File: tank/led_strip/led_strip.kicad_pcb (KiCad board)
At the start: 2 copper layers, 50.5 x 10.8 mm, 9 parts, among them J1 Conn_01x04_Male

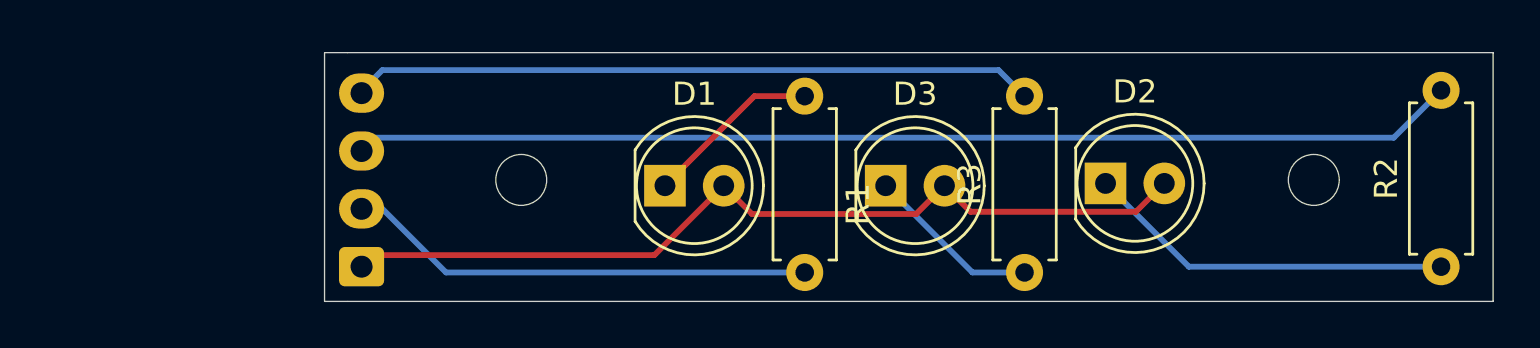
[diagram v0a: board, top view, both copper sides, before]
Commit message: LED Strip v0.5 - Change LED strip from 3 LEDs to 4
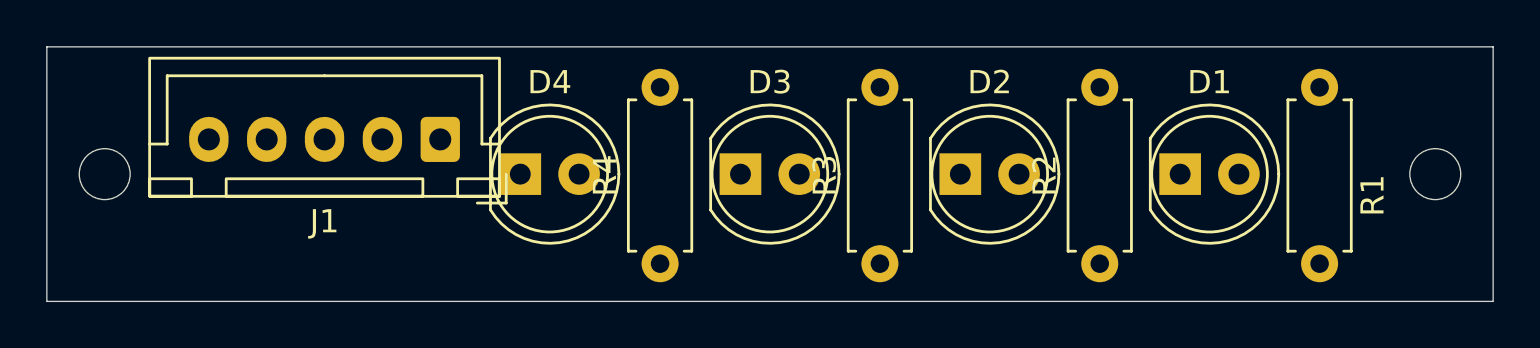
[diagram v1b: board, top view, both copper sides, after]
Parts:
- removed REF** (x2): MountingHole_2.2mm_M2, MountingHole:MountingHole_2.2mm_M2
- added D4: LED, custom:LED_D5.0mm, F.Cu at (101.5, 97.5)
- added H1: MountingHole, MountingHole:MountingHole_2.2mm_M2, F.Cu at (83.5, 97.5)
- added H2: MountingHole, MountingHole:MountingHole_2.2mm_M2, F.Cu at (141.0, 97.5)
- added R4: R, custom:R_Axial_DIN0207_L6.3mm_D2.5mm_P7.62mm_Horizontal, F.Cu at (107.5, 101.4)
- J1: value Conn_01x04_Male -> Conn_01x05_Pin; footprint custom:JST_EH_B4B-EH-A_1x04_P2.50mm_Vertical -> Connector_JST:JST_XH_B5B-XH-A_1x05_P2.50mm_Vertical; moved to F.Cu
- moved D1 22.3 mm to (130.0, 97.5)
- moved R1 22.3 mm to (136.0, 93.8)
- moved R2 14.8 mm to (126.5, 101.4)
- moved J1 6.47 mm to (98.0, 96.0), turned to 180 degrees
- moved D3 6.29 mm to (111.0, 97.5)
- moved D2 6.29 mm to (120.5, 97.5)
- moved R3 6.26 mm to (117.0, 101.4)
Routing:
- net Net-(J1-Pin_3): track 47.1 -> 0.00 mm
- net Net-(D1-A): track 37.5 -> 0.00 mm
- net Net-(J1-Pin_4): track 28.9 -> 0.00 mm
- net Net-(J1-Pin_2): track 20.1 -> 0.00 mm
- net Net-(D2-K): track 16.0 -> 0.00 mm
- net Net-(D1-K): track 7.64 -> 0.00 mm
- net Net-(D3-K): track 7.55 -> 0.00 mm
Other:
- board size 50.5 x 10.8 mm -> 62.5 x 11 mm
- net class Default removed
- board text added: "LED Strip Version 0.5"
- board text removed: "LED Strip Version 0.4"

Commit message: whoops!
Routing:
- net Net-(J1-Pin_2): track 0.00 -> 42.7 mm
- net Net-(D1-A): track 0.00 -> 41.5 mm
- net Net-(J1-Pin_3): track 0.00 -> 35.4 mm
- net Net-(J1-Pin_4): track 0.00 -> 27.6 mm
- net Net-(J1-Pin_5): track 0.00 -> 20.4 mm
- net Net-(D4-K): track 0.00 -> 7.64 mm
- net Net-(D3-K): track 0.00 -> 7.63 mm
- net Net-(D2-K): track 0.00 -> 7.63 mm
- net Net-(D1-K): track 0.00 -> 7.58 mm
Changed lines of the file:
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@@
 		)
+	)
+	(segment
+		(start 104 97.5)
+		(end 102.5 96)
+		(width 0.25)
+		(layer "F.Cu")
+		(net 1)
+	)
+	(segment
+		(start 113.515 97.5)
+		(end 112.015 96)
+		(width 0.25)
+		(layer "F.Cu")
+		(net 1)
+	)
+	(segment
+		(start 112.015 96)
+		(end 121.515 96)
+		(width 0.25)
+		(layer "F.Cu")
+		(net 1)
+	)
+	(segment
+		(start 121.515 96)
+		(end 123.015 97.5)
+		(width 0.25)
+		(layer "F.Cu")
+		(net 1)
+	)
+	(segment
+		(start 112.015 96)
+		(end 102.5 96)
+		(width 0.25)
+		(layer "F.Cu")
+		(net 1)
+	)
+	(segment
+		(start 102.5 96)
+		(end 98 96)
+		(width 0.25)
+		(layer "F.Cu")
+		(net 1)
+	)
+	(segment
+		(start 131.015 96)
+		(end 132.515 97.5)
+		(width 0.25)
+		(layer "F.Cu")
+		(net 1)
+	)
+	(segment
+		(start 121.515 96)
+		(end 131.015 96)
+		(width 0.25)
+		(layer "F.Cu")
+		(net 1)
+	)
+	(segment
+		(start 133.725 93.75)
+		(end 136 93.75)
+		(width 0.25)
+		(layer "B.Cu")
+		(net 2)
+	)
+	(segment
+		(start 129.975 97.5)
+		(end 133.725 93.75)
+		(width 0.25)
+		(layer "B.Cu")
+		(net 2)
+	)
+	(segment
+		(start 124.345 101.37)
+		(end 126.5 101.37)
+		(width 0.25)
+		(layer "F.Cu")
+		(net 3)
+	)
+	(segment
+		(start 120.475 97.5)
+		(end 124.345 101.37)
+		(width 0.25)
+		(layer "F.Cu")
+		(net 3)
+	)
+	(segment
+		(start 110.975 97.5)
+		(end 114.845 101.37)
+		(width 0.25)
+		(layer "F.Cu")
+		(net 4)
+	)
+	(segment
+		(start 114.845 101.37)
+		(end 117 101.37)
+		(width 0.25)
+		(layer "F.Cu")
+		(net 4)
+	)
+	(segment
+		(start 105.33 101.37)
+		(end 107.5 101.37)
+		(width 0.25)
+		(layer "F.Cu")
+		(net 5)
+	)
+	(segment
+		(start 101.46 97.5)
+		(end 105.33 101.37)
+		(width 0.25)
+		(layer "F.Cu")
+		(net 5)
+	)
+	(segment
+		(start 99.744 100.244)
+		(end 95.5 96)
+		(width 0.25)
+		(layer "B.Cu")
+		(net 6)
+	)
+	(segment
+		(start 136 101.37)
+		(end 134.874 100.244)
+		(width 0.25)
+		(layer "B.Cu")
+		(net 6)
+	)
+	(segment
+		(start 134.874 100.244)
+		(end 99.744 100.244)
+		(width 0.25)
+		(layer "B.Cu")
+		(net 6)
+	)
+	(segment
+		(start 93 96)
+		(end 96.376 92.624)
+		(width 0.25)
+		(layer "B.Cu")
+		(net 7)
+	)
+	(segment
+		(start 96.376 92.624)
+		(end 125.374 92.624)
+		(width 0.25)
+		(layer "B.Cu")
+		(net 7)
+	)
+	(segment
+		(start 125.374 92.624)
+		(end 126.5 93.75)
+		(width 0.25)
+		(layer "B.Cu")
+		(net 7)
+	)
+	(segment
+		(start 91.801 94.699)
+		(end 106.856595 94.699)
+		(width 0.25)
+		(layer "F.Cu")
+		(net 8)
+	)
+	(segment
+		(start 107.033595 94.876)
+		(end 115.874 94.876)
+		(width 0.25)
+		(layer "F.Cu")
+		(net 8)
+	)
+	(segment
+		(start 115.874 94.876)
+		(end 117 93.75)
+		(width 0.25)
+		(layer "F.Cu")
+		(net 8)
+	)
+	(segment
+		(start 106.856595 94.699)
+		(end 107.033595 94.876)
+		(width 0.25)
+		(layer "F.Cu")
+		(net 8)
+	)
+	(segment
+		(start 90.5 96)
+		(end 91.801 94.699)
+		(width 0.25)
+		(layer "F.Cu")
+		(net 8)
+	)
+	(segment
+		(start 88 96)
+		(end 90.25 93.75)
+		(width 0.25)
+		(layer "F.Cu")
+		(net 9)
+	)
+	(segment
+		(start 90.25 93.75)
+		(end 107.5 93.75)
+		(width 0.25)
+		(layer "F.Cu")
+		(net 9)
 	)
 	(embedded_fonts no)

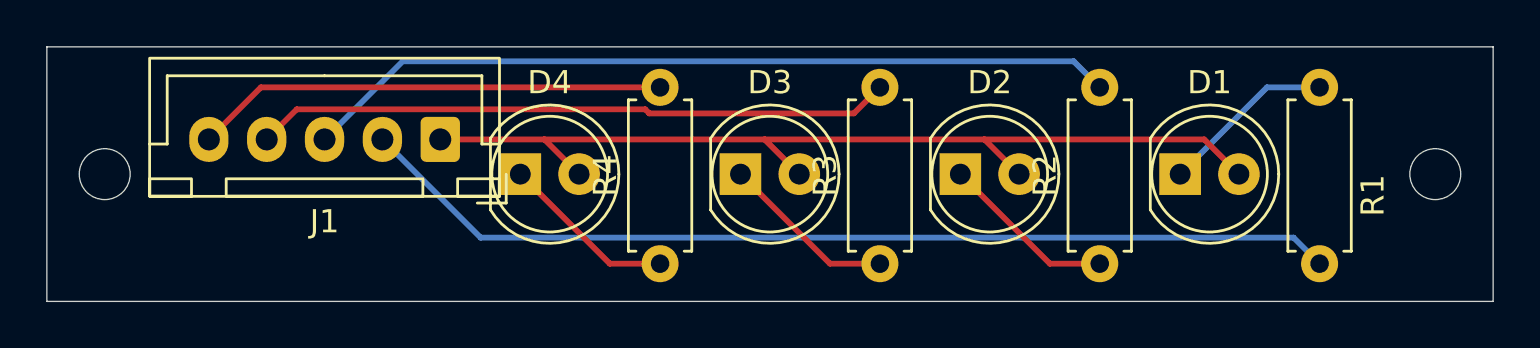
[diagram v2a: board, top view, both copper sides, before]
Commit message: LED Strip v0.6
Different spacing for LEDs
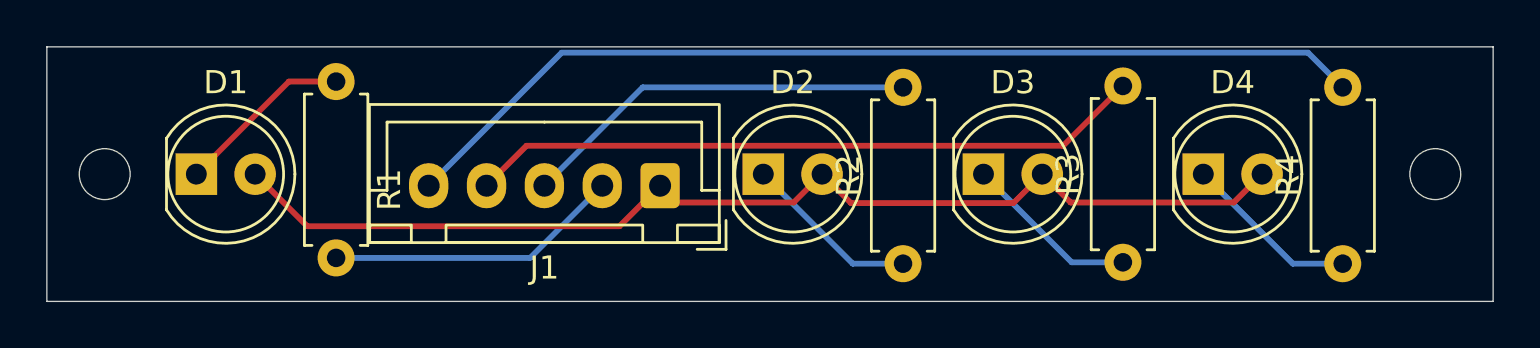
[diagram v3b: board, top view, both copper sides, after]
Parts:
- moved D1 42.5 mm to (87.5, 97.5)
- moved R1 42.5 mm to (93.5, 93.5)
- moved D4 29.5 mm to (131.0, 97.5)
- moved R4 29.5 mm to (137.0, 101.4)
- moved R3 10.5 mm to (127.5, 101.3)
- moved D3 10.5 mm to (121.5, 97.5)
- moved J1 9.71 mm to (107.5, 98.0)
- moved D2 8.52 mm to (112.0, 97.5)
- moved R2 8.50 mm to (118.0, 101.4)
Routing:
- net Net-(J1-Pin_2): track 42.7 -> 12.8 mm
- net Net-(J1-Pin_5): track 20.4 -> 42.5 mm
- net Net-(J1-Pin_3): track 35.4 -> 17.3 mm
- net Net-(D1-A): track 41.5 -> 48.0 mm
- net Net-(J1-Pin_4): track 27.6 -> 29.3 mm
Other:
- board text added: "LED Strip Version 0.6"
- board text removed: "LED Strip Version 0.5"
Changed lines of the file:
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@@
 	(footprint "custom:LED_D5.0mm"
 		(layer "F.Cu")
-		(at 129.975 97.5)
+		(at 87.46 97.5)
 		(descr "LED, diameter 5.0mm, 2 pins, http://cdn-reichelt.de/documents/datenblatt/A500/LL-504BC2E-009.pdf")
 		(tags "LED diameter 5.0mm 2 pins")
@@
 	(footprint "custom:LED_D5.0mm"
 		(layer "F.Cu")
-		(at 120.475 97.5)
+		(at 111.96 97.5)
 		(descr "LED, diameter 5.0mm, 2 pins, http://cdn-reichelt.de/documents/datenblatt/A500/LL-504BC2E-009.pdf")
 		(tags "LED diameter 5.0mm 2 pins")
@@
 	(footprint "custom:LED_D5.0mm"
 		(layer "F.Cu")
-		(at 110.975 97.5)
+		(at 121.475 97.5)
 		(descr "LED, diameter 5.0mm, 2 pins, http://cdn-reichelt.de/documents/datenblatt/A500/LL-504BC2E-009.pdf")
 		(tags "LED diameter 5.0mm 2 pins")
@@
 	(footprint "custom:R_Axial_DIN0207_L6.3mm_D2.5mm_P7.62mm_Horizontal"
 		(layer "F.Cu")
-		(at 136 93.75 -90)
+		(at 93.5 93.5 -90)
 		(descr "Resistor, Axial_DIN0207 series, Axial, Horizontal, pin pitch=7.62mm, 0.25W = 1/4W, length*diameter=6.3*2.5mm^2, http://cdn-reichelt.de/documents/datenblatt/B400/1_4W%23YAG.pdf")
 		(tags "Resistor Axial_DIN0207 series Axial Horizontal pin pitch 7.62mm 0.25W = 1/4W length 6.3mm diameter 2.5mm")
@@
 	(footprint "custom:R_Axial_DIN0207_L6.3mm_D2.5mm_P7.62mm_Horizontal"
 		(layer "F.Cu")
-		(at 126.5 101.37 90)
+		(at 118 101.37 90)
 		(descr "Resistor, Axial_DIN0207 series, Axial, Horizontal, pin pitch=7.62mm, 0.25W = 1/4W, length*diameter=6.3*2.5mm^2, http://cdn-reichelt.de/documents/datenblatt/B400/1_4W%23YAG.pdf")
 		(tags "Resistor Axial_DIN0207 series Axial Horizontal pin pitch 7.62mm 0.25W = 1/4W length 6.3mm diameter 2.5mm")
@@
 	(footprint "custom:R_Axial_DIN0207_L6.3mm_D2.5mm_P7.62mm_Horizontal"
 		(layer "F.Cu")
-		(at 117 101.37 90)
+		(at 127.5 101.31 90)
 		(descr "Resistor, Axial_DIN0207 series, Axial, Horizontal, pin pitch=7.62mm, 0.25W = 1/4W, length*diameter=6.3*2.5mm^2, http://cdn-reichelt.de/documents/datenblatt/B400/1_4W%23YAG.pdf")
 		(tags "Resistor Axial_DIN0207 series Axial Horizontal pin pitch 7.62mm 0.25W = 1/4W length 6.3mm diameter 2.5mm")
@@
 	(footprint "custom:R_Axial_DIN0207_L6.3mm_D2.5mm_P7.62mm_Horizontal"
 		(layer "F.Cu")
-		(at 107.5 101.37 90)
+		(at 137 101.37 90)
 		(descr "Resistor, Axial_DIN0207 series, Axial, Horizontal, pin pitch=7.62mm, 0.25W = 1/4W, length*diameter=6.3*2.5mm^2, http://cdn-reichelt.de/documents/datenblatt/B400/1_4W%23YAG.pdf")
 		(tags "Resistor Axial_DIN0207 series Axial Horizontal pin pitch 7.62mm 0.25W = 1/4W length 6.3mm diameter 2.5mm")
@@
 	(footprint "Connector_JST:JST_XH_B5B-XH-A_1x05_P2.50mm_Vertical"
 		(layer "F.Cu")
-		(at 98 96 180)
+		(at 107.5 98 180)
 		(descr "JST XH series connector, B5B-XH-A (http://www.jst-mfg.com/product/pdf/eng/eXH.pdf), generated with kicad-footprint-generator")
 		(tags "connector JST XH vertical")
@@
 	(footprint "custom:LED_D5.0mm"
 		(layer "F.Cu")
-		(at 101.46 97.5)
+		(at 130.975 97.5)
 		(descr "LED, diameter 5.0mm, 2 pins, http://cdn-reichelt.de/documents/datenblatt/A500/LL-504BC2E-009.pdf")
 		(tags "LED diameter 5.0mm 2 pins")
@@
 		(layer "Edge.Cuts")
 	)
-	(gr_text "LED Strip Version 0.5"
+	(gr_text "LED Strip Version 0.6"
 		(at 120.75 99.5 0)
 		(layer "B.SilkS")
@@
 	)
 	(segment
-		(start 104 97.5)
-		(end 102.5 96)
+		(start 108.226 98.726)
+		(end 113.274 98.726)
 		(width 0.25)
 		(layer "F.Cu")
@@
 	)
 	(segment
-		(start 113.515 97.5)
-		(end 112.015 96)
+		(start 124.015 97.5)
+		(end 125.241 98.726)
 		(width 0.25)
 		(layer "F.Cu")
@@
 	)
 	(segment
-		(start 112.015 96)
-		(end 121.515 96)
+		(start 132.289 98.726)
+		(end 133.515 97.5)
 		(width 0.25)
 		(layer "F.Cu")
@@
 	)
 	(segment
-		(start 121.515 96)
-		(end 123.015 97.5)
+		(start 92.25 99.75)
+		(end 105.75 99.75)
 		(width 0.25)
 		(layer "F.Cu")
@@
 	)
 	(segment
-		(start 112.015 96)
-		(end 102.5 96)
+		(start 122.765 98.75)
+		(end 124.015 97.5)
 		(width 0.25)
 		(layer "F.Cu")
@@
 	)
 	(segment
-		(start 102.5 96)
-		(end 98 96)
+		(start 105.75 99.75)
+		(end 107.5 98)
 		(width 0.25)
 		(layer "F.Cu")
@@
 	)
 	(segment
-		(start 131.015 96)
-		(end 132.515 97.5)
+		(start 107.5 98)
+		(end 108.226 98.726)
 		(width 0.25)
 		(layer "F.Cu")
@@
 	)
 	(segment
-		(start 121.515 96)
-		(end 131.015 96)
+		(start 125.241 98.726)
+		(end 132.289 98.726)
 		(width 0.25)
 		(layer "F.Cu")
@@
 	)
 	(segment
-		(start 133.725 93.75)
-		(end 136 93.75)
+		(start 90 97.5)
+		(end 92.25 99.75)
+		(width 0.25)
+		(layer "F.Cu")
+		(net 1)
+	)
+	(segment
+		(start 115.75 98.75)
+		(end 122.765 98.75)
+		(width 0.25)
+		(layer "F.Cu")
+		(net 1)
+	)
+	(segment
+		(start 114.5 97.5)
+		(end 115.75 98.75)
+		(width 0.25)
+		(layer "F.Cu")
+		(net 1)
+	)
+	(segment
+		(start 113.274 98.726)
+		(end 114.5 97.5)
+		(width 0.25)
+		(layer "F.Cu")
+		(net 1)
+	)
+	(segment
+		(start 87.46 97.5)
+		(end 91.46 93.5)
+		(width 0.25)
+		(layer "F.Cu")
+		(net 2)
+	)
+	(segment
+		(start 91.46 93.5)
+		(end 93.5 93.5)
+		(width 0.25)
+		(layer "F.Cu")
+		(net 2)
+	)
+	(segment
+		(start 111.96 97.5)
+		(end 115.83 101.37)
 		(width 0.25)
 		(layer "B.Cu")
-		(net 2)
-	)
-	(segment
-		(start 129.975 97.5)
-		(end 133.725 93.75)
+		(net 3)
+	)
+	(segment
+		(start 115.83 101.37)
+		(end 118 101.37)
 		(width 0.25)
 		(layer "B.Cu")
-		(net 2)
-	)
-	(segment
-		(start 124.345 101.37)
-		(end 126.5 101.37)
-		(width 0.25)
-		(layer "F.Cu")
 		(net 3)
 	)
 	(segment
-		(start 120.475 97.5)
-		(end 124.345 101.37)
-		(width 0.25)
-		(layer "F.Cu")
-		(net 3)
-	)
-	(segment
-		(start 110.975 97.5)
-		(end 114.845 101.37)
-		(width 0.25)
-		(layer "F.Cu")
+		(start 121.475 97.5)
+		(end 125.285 101.31)
+		(width 0.25)
+		(layer "B.Cu")
 		(net 4)
 	)
 	(segment
-		(start 114.845 101.37)
-		(end 117 101.37)
-		(width 0.25)
-		(layer "F.Cu")
+		(start 125.285 101.31)
+		(end 127.5 101.31)
+		(width 0.25)
+		(layer "B.Cu")
 		(net 4)
 	)
 	(segment
-		(start 105.33 101.37)
-		(end 107.5 101.37)
-		(width 0.25)
-		(layer "F.Cu")
+		(start 130.975 97.5)
+		(end 134.845 101.37)
+		(width 0.25)
+		(layer "B.Cu")
 		(net 5)
 	)
 	(segment
-		(start 101.46 97.5)
-		(end 105.33 101.37)
-		(width 0.25)
-		(layer "F.Cu")
+		(start 134.845 101.37)
+		(end 137 101.37)
+		(width 0.25)
+		(layer "B.Cu")
 		(net 5)
 	)
 	(segment
-		(start 99.744 100.244)
-		(end 95.5 96)
+		(start 101.88 101.12)
+		(end 105 98)
 		(width 0.25)
 		(layer "B.Cu")
@@
 	)
 	(segment
-		(start 136 101.37)
-		(end 134.874 100.244)
+		(start 93.5 101.12)
+		(end 101.88 101.12)
 		(width 0.25)
 		(layer "B.Cu")
@@
 	)
 	(segment
-		(start 134.874 100.244)
-		(end 99.744 100.244)
-		(width 0.25)
-		(layer "B.Cu")
-		(net 6)
-	)
-	(segment
-		(start 93 96)
-		(end 96.376 92.624)
+		(start 106.75 93.75)
+		(end 118 93.75)
 		(width 0.25)
 		(layer "B.Cu")
@@
 	)
 	(segment
-		(start 96.376 92.624)
-		(end 125.374 92.624)
+		(start 102.5 98)
+		(end 106.75 93.75)
 		(width 0.25)
 		(layer "B.Cu")
@@
 	)
 	(segment
-		(start 125.374 92.624)
-		(end 126.5 93.75)
+		(start 124.916 96.274)
+		(end 127.5 93.69)
+		(width 0.25)
+		(layer "F.Cu")
+		(net 8)
+	)
+	(segment
+		(start 101.726 96.274)
+		(end 124.916 96.274)
+		(width 0.25)
+		(layer "F.Cu")
+		(net 8)
+	)
+	(segment
+		(start 100 98)
+		(end 101.726 96.274)
+		(width 0.25)
+		(layer "F.Cu")
+		(net 8)
+	)
+	(segment
+		(start 97.5 98)
+		(end 103.25 92.25)
 		(width 0.25)
 		(layer "B.Cu")
-		(net 7)
-	)
-	(segment
-		(start 91.801 94.699)
-		(end 106.856595 94.699)
-		(width 0.25)
-		(layer "F.Cu")
-		(net 8)
-	)
-	(segment
-		(start 107.033595 94.876)
-		(end 115.874 94.876)
-		(width 0.25)
-		(layer "F.Cu")
-		(net 8)
-	)
-	(segment
-		(start 115.874 94.876)
-		(end 117 93.75)
-		(width 0.25)
-		(layer "F.Cu")
-		(net 8)
-	)
-	(segment
-		(start 106.856595 94.699)
-		(end 107.033595 94.876)
-		(width 0.25)
-		(layer "F.Cu")
-		(net 8)
-	)
-	(segment
-		(start 90.5 96)
-		(end 91.801 94.699)
-		(width 0.25)
-		(layer "F.Cu")
-		(net 8)
-	)
-	(segment
-		(start 88 96)
-		(end 90.25 93.75)
-		(width 0.25)
-		(layer "F.Cu")
 		(net 9)
 	)
 	(segment
-		(start 90.25 93.75)
-		(end 107.5 93.75)
-		(width 0.25)
-		(layer "F.Cu")
+		(start 103.25 92.25)
+		(end 135.5 92.25)
+		(width 0.25)
+		(layer "B.Cu")
 		(net 9)
 	)
+	(segment
+		(start 135.5 92.25)
+		(end 137 93.75)
+		(width 0.25)
+		(layer "B.Cu")
+		(net 9)
+	)
